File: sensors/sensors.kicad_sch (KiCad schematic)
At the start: 9 parts, among them J1 GPIO, J2 JP_CAN, J3 JP_PWM, J4 JP_ADC

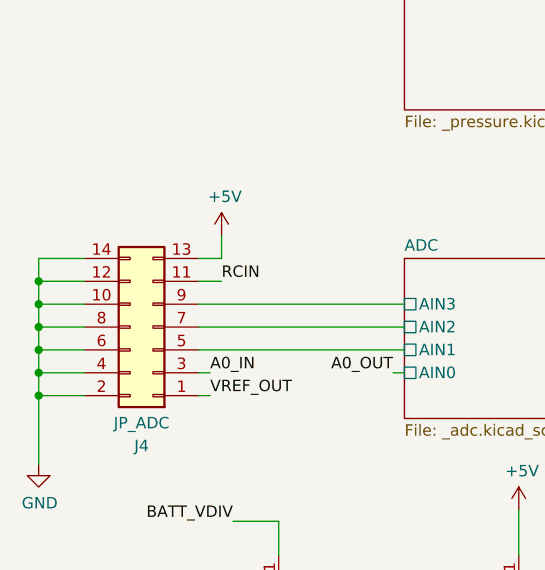
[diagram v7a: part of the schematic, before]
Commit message: use 2x8 for ADC header; added part numbers
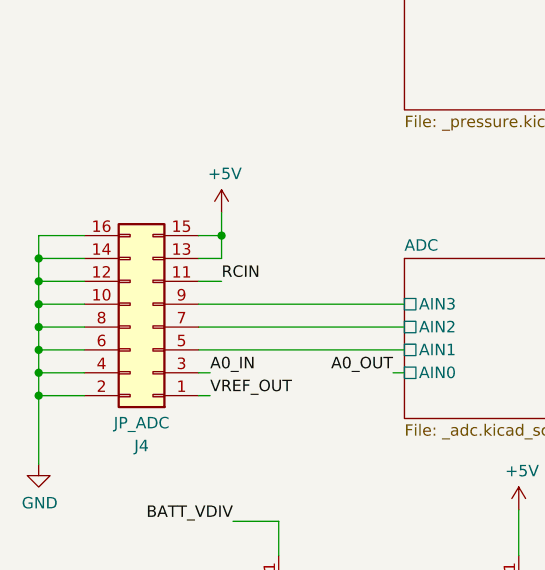
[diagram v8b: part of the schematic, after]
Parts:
- J2: Part (none) -> 1.25-4PWTDK
- J3: Part (none) -> ZX-PZ2.54-1-16PZZ
- J4: footprint Connector_PinHeader_2.54mm:PinHeader_2x07_P2.54mm_Horizontal -> Connector_PinHeader_2.54mm:PinHeader_2x08_P2.54mm_Horizontal; symbol Connector_Generic:Conn_02x07_Odd_Even -> Connector_Generic:Conn_02x08_Odd_Even; Part (none) -> PZ254R-12-16P
- R33, R34: Part C25744 -> 0402WGF3301TCE
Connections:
- net +5V: now also J4.15 (Pin_15)
- net GND: now also J4.16 (Pin_16)
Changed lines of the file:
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@@
 	)
 	(junction
+		(at 21.59 214.63)
+		(diameter 0)
+		(color 0 0 0 0)
+	)
+	(junction
 		(at 58.42 67.31)
 		(diameter 1.016)
@@
 	)
 	(junction
+		(at 41.91 212.09)
+		(diameter 0)
+		(color 0 0 0 0)
+	)
+	(junction
 		(at 76.2 72.39)
 		(diameter 1.016)
@@
 	(wire
 		(pts
+			(xy 41.91 214.63) (xy 39.37 214.63)
+		)
+		(stroke
+			(width 0)
+			(type default)
+		)
+	)
+	(wire
+		(pts
 			(xy 29.21 135.89) (xy 36.83 135.89)
 		)
@@
 	(wire
 		(pts
+			(xy 41.91 212.09) (xy 41.91 214.63)
+		)
+		(stroke
+			(width 0)
+			(type default)
+		)
+	)
+	(wire
+		(pts
 			(xy 21.59 217.17) (xy 21.59 219.71)
 		)
@@
 	(wire
 		(pts
+			(xy 41.91 209.55) (xy 41.91 212.09)
+		)
+		(stroke
+			(width 0)
+			(type default)
+		)
+	)
+	(wire
+		(pts
 			(xy 73.66 44.45) (xy 106.68 44.45)
 		)
@@
 	(wire
 		(pts
+			(xy 39.37 212.09) (xy 41.91 212.09)
+		)
+		(stroke
+			(width 0)
+			(type default)
+		)
+	)
+	(wire
+		(pts
 			(xy 29.21 123.19) (xy 36.83 123.19)
 		)
@@
 	(wire
 		(pts
+			(xy 21.59 212.09) (xy 21.59 214.63)
+		)
+		(stroke
+			(width 0)
+			(type default)
+		)
+	)
+	(wire
+		(pts
 			(xy 21.59 222.25) (xy 26.67 222.25)
 		)
@@
 	(wire
 		(pts
+			(xy 26.67 212.09) (xy 21.59 212.09)
+		)
+		(stroke
+			(width 0)
+			(type default)
+		)
+	)
+	(wire
+		(pts
 			(xy 73.66 49.53) (xy 106.68 49.53)
 		)
@@
 	(wire
 		(pts
-			(xy 39.37 214.63) (xy 41.91 214.63)
-		)
-		(stroke
-			(width 0)
-			(type default)
-		)
-	)
-	(wire
-		(pts
 			(xy 21.59 219.71) (xy 26.67 219.71)
 		)
@@
 	(wire
 		(pts
-			(xy 41.91 214.63) (xy 41.91 212.09)
-		)
-		(stroke
-			(width 0)
-			(type default)
-		)
-	)
-	(wire
-		(pts
 			(xy 58.42 85.09) (xy 60.96 85.09)
 		)
@@
 			)
 		)
-		(property "Part" "C25744"
+		(property "Part" "0402WGF3301TCE"
 			(at 173.99 45.72 0)
 			(hide yes)
@@
 			)
 		)
-		(property "Part" "C25744"
+		(property "Part" "0402WGF3301TCE"
 			(at 165.1 45.72 0)
 			(hide yes)
@@
 			)
 		)
+		(property "Part" "ZX-PZ2.54-1-16PZZ"
+			(at 24.13 138.43 0)
+			(hide yes)
+			(show_name no)
+			(do_not_autoplace no)
+			(effects
+				(font
+					(size 1.27 1.27)
+				)
+			)
+		)
 		(pin "6"
 		)
@@
 	(symbol
 		(lib_id "power:+5V")
-		(at 41.91 212.09 0)
+		(at 41.91 209.55 0)
 		(unit 1)
 		(body_style 1)
@@
 		(dnp no)
 		(property "Reference" "#PWR070"
-			(at 41.91 215.9 0)
+			(at 41.91 213.36 0)
 			(hide yes)
 			(show_name no)
@@
 		)
 		(property "Value" "+5V"
-			(at 42.2783 207.7656 0)
+			(at 42.2783 205.2256 0)
 			(show_name no)
 			(do_not_autoplace no)
@@
 		)
 		(property "Footprint" ""
-			(at 41.91 212.09 0)
+			(at 41.91 209.55 0)
 			(show_name no)
 			(do_not_autoplace no)
@@
 		)
 		(property "Datasheet" ""
-			(at 41.91 212.09 0)
+			(at 41.91 209.55 0)
 			(show_name no)
 			(do_not_autoplace no)
@@
 		)
 		(property "Description" "Power symbol creates a global label with name \"+5V\""
-			(at 41.91 212.09 0)
+			(at 41.91 209.55 0)
 			(hide yes)
 			(show_name no)
@@
 	)
 	(symbol
-		(lib_id "Connector_Generic:Conn_02x07_Odd_Even")
+		(lib_id "Connector_Generic:Conn_02x08_Odd_Even")
 		(at 34.29 222.25 180)
 		(unit 1)
@@
 			)
 		)
-		(property "Footprint" "Connector_PinHeader_2.54mm:PinHeader_2x07_P2.54mm_Horizontal"
+		(property "Footprint" "Connector_PinHeader_2.54mm:PinHeader_2x08_P2.54mm_Horizontal"
 			(at 34.29 222.25 0)
 			(hide yes)
@@
 			)
 		)
-		(property "Description" "Generic connector, double row, 02x07, odd/even pin numbering scheme (row 1 odd numbers, row 2 even numbers), script generated (kicad-library-utils/schlib/autogen/connector/)"
+		(property "Description" "Generic connector, double row, 02x08, odd/even pin numbering scheme (row 1 odd numbers, row 2 even numbers), script generated (kicad-library-utils/schlib/autogen/connector/)"
 			(at 34.29 222.25 0)
 			(hide yes)
@@
 			)
 		)
-		(property "Part" ""
+		(property "Part" "PZ254R-12-16P"
 			(at 34.29 222.25 0)
 			(hide yes)
@@
 		(pin "13"
 		)
+		(pin "15"
+		)
+		(pin "16"
+		)
 		(instances
 			(project "sensors"
@@
 			)
 		)
-		(property "Part" ""
+		(property "Part" "1.25-4PWTDK"
 			(at 130.81 152.4 0)
 			(hide yes)
